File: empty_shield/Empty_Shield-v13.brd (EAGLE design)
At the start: 101.6 x 53.3 mm, 18 parts

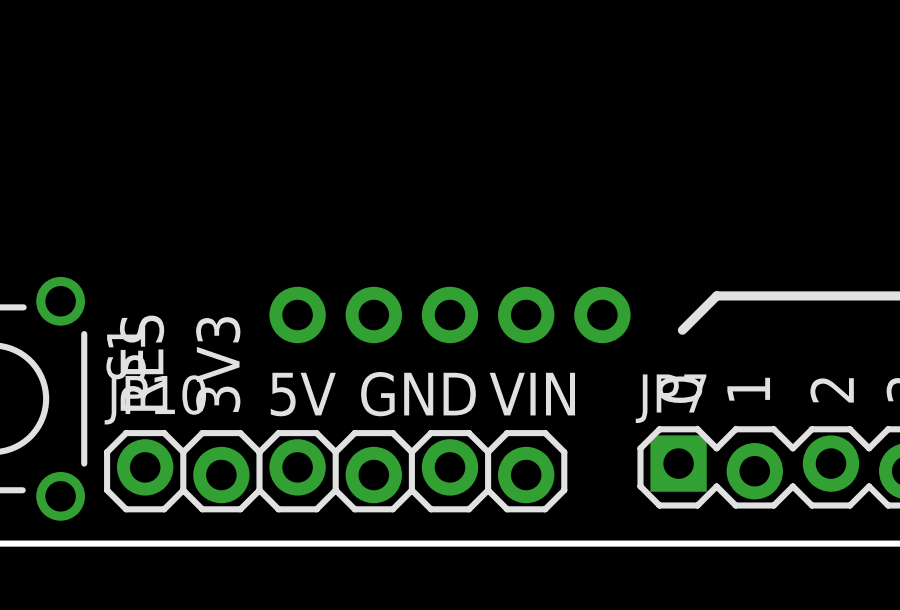
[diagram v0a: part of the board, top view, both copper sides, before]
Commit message: empty shield SMD
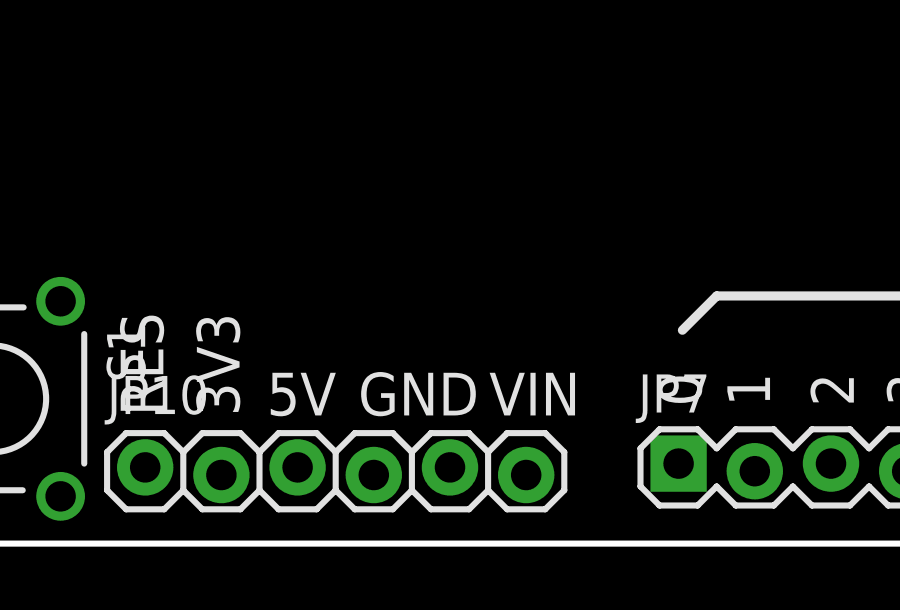
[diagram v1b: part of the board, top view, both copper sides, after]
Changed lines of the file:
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@@
 <wire x1="2.54" y1="5.08" x2="15.24" y2="10.16" width="0" layer="19" extent="1-1"/>
-</signal>
-<signal name="N$319">
-<via x="38.1" y="7.62" extent="1-16" drill="1.016" diameter="1.8796"/>
-</signal>
-<signal name="N$320">
-<via x="40.64" y="7.62" extent="1-16" drill="1.016" diameter="1.8796"/>
-</signal>
-<signal name="N$321">
-<via x="43.18" y="7.62" extent="1-16" drill="1.016" diameter="1.8796"/>
-</signal>
-<signal name="N$322">
-<via x="48.26" y="7.62" extent="1-16" drill="1.016" diameter="1.8796"/>
-</signal>
-<signal name="N$323">
-<via x="45.72" y="7.62" extent="1-16" drill="1.016" diameter="1.8796"/>
 </signal>
 </signals>
